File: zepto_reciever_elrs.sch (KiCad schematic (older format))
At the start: 50 parts, among them J1 u.fl, SW1 SW_Push, U1 STM32WLE5JBI6, U2 NCP160, U3 BGS12PL6E6327XTSA1, Y1 32MHz

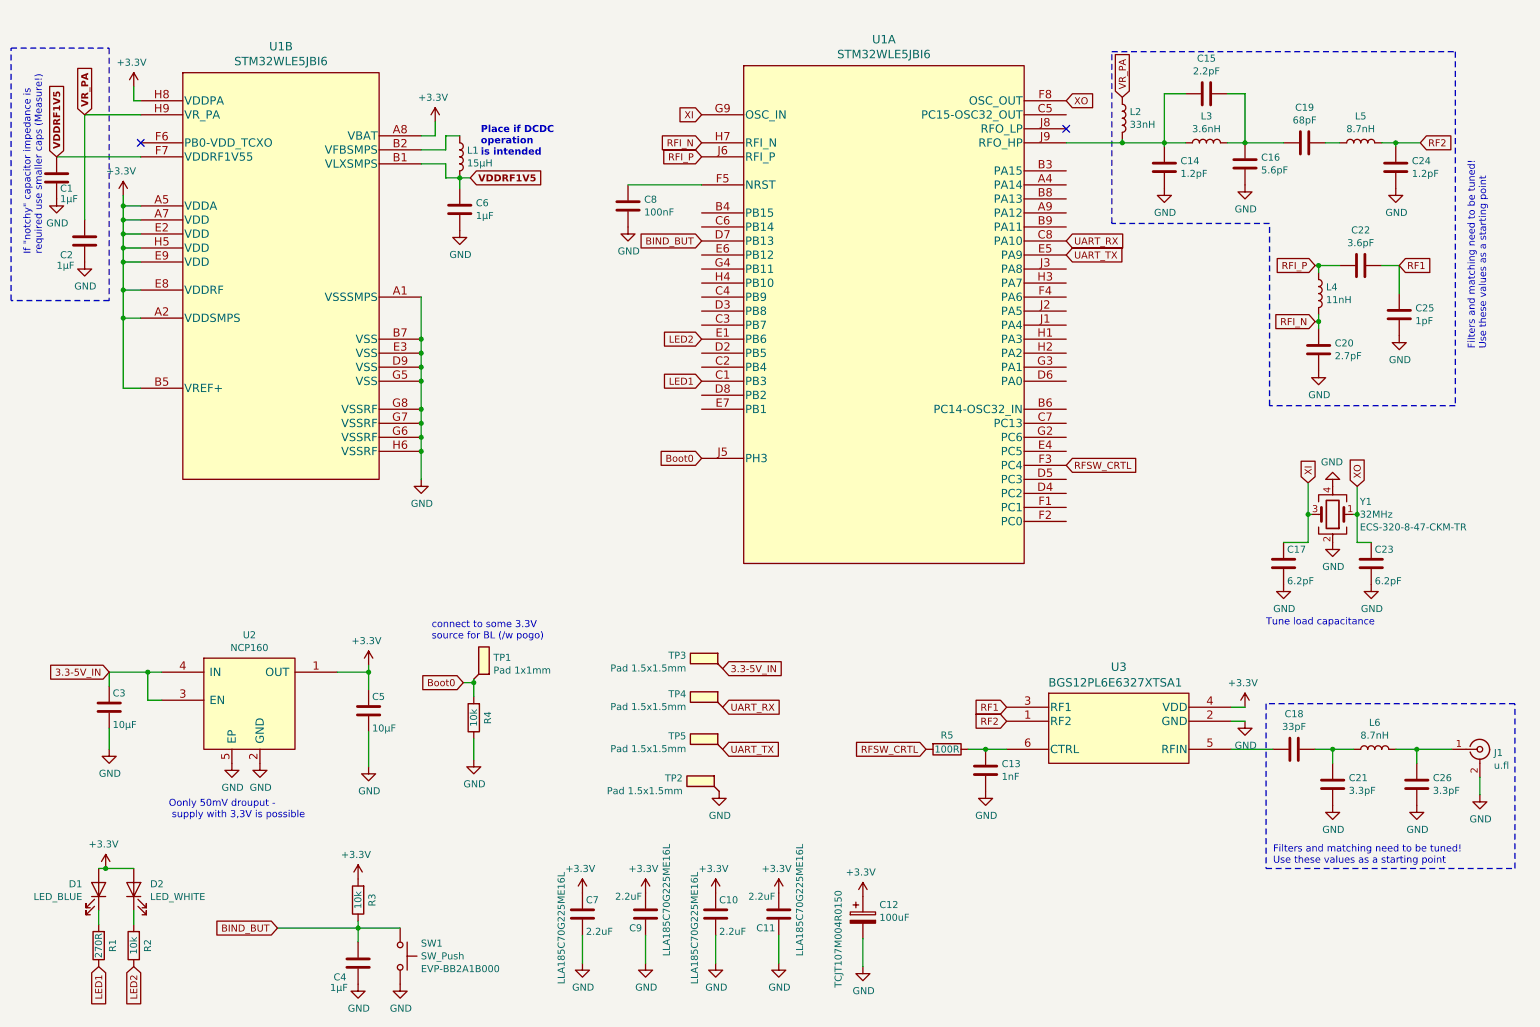
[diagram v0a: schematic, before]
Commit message: Routed half of the Layout, changed a few pins
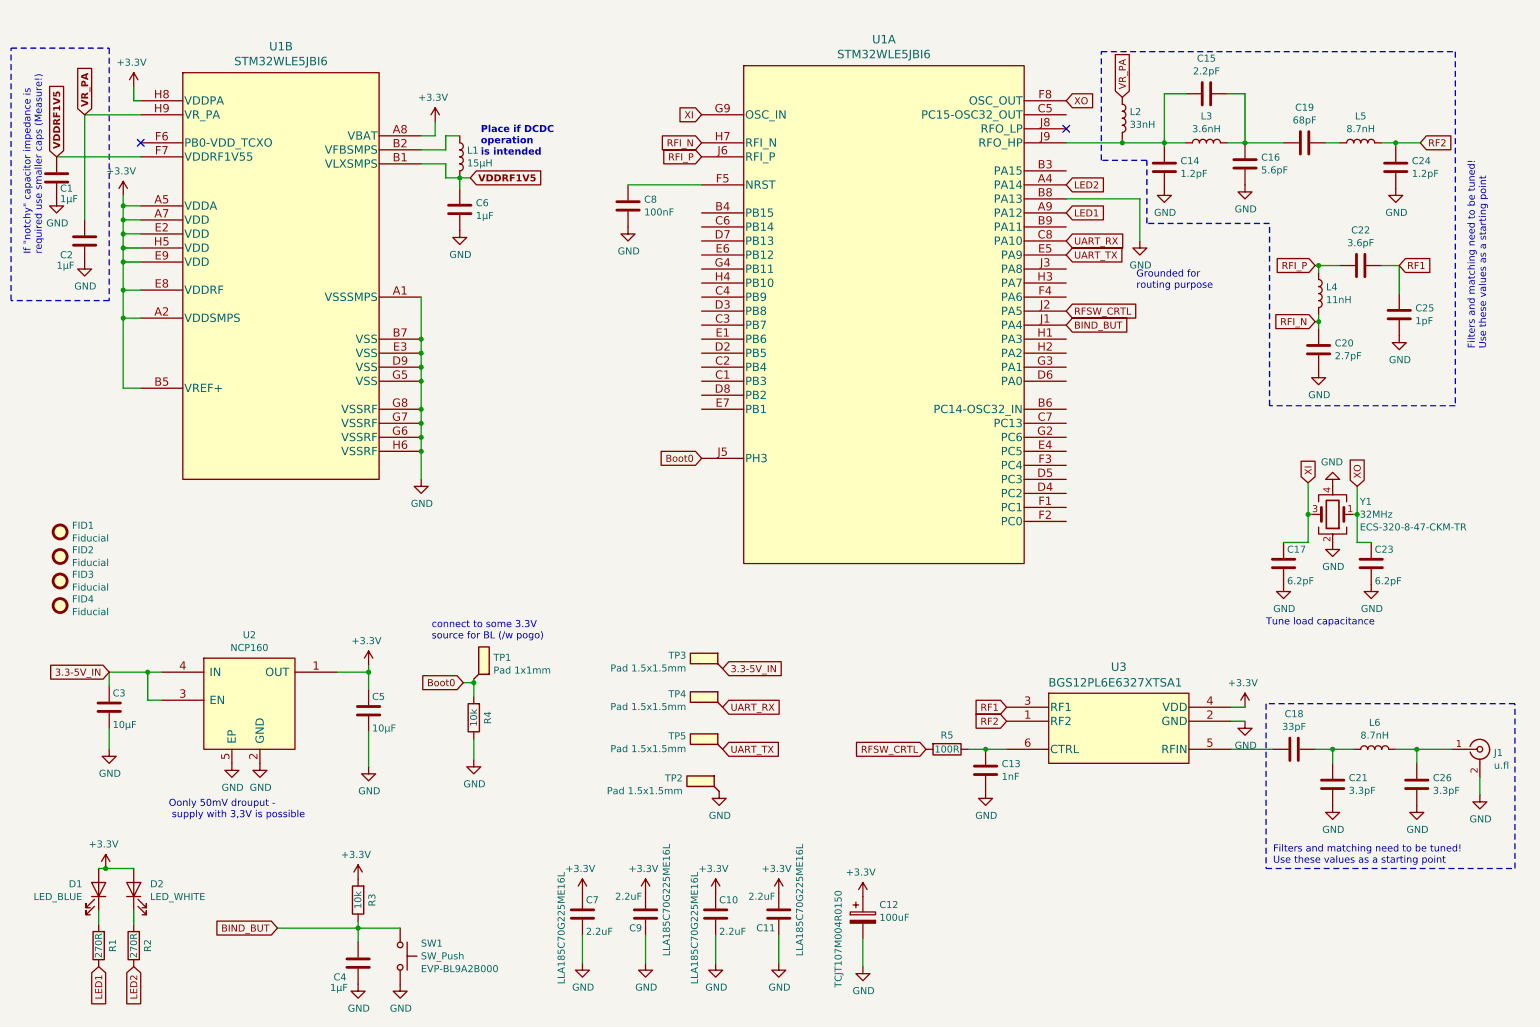
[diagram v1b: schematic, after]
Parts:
- added FID1, FID2, FID3, FID4: Fiducial, Fiducial:Fiducial_0.5mm_Dia_1mm_Outer, symbol Mechanical:Fiducial
- D1: footprint LED_SMD:LED_0201_0603Metric -> LED_SMD:LED_0402_1005Metric; BomCos@10k 0,057 -> 0,059; Type SML-LX0201USBC-TR -> VLMB1500-GS08
- D2: footprint LED_SMD:LED_0201_0603Metric -> LED_SMD:LED_0402_1005Metric; BomCos@10k 0,062 -> 0,053; Type SML-LX0201NWD-TR -> LW QH8G-Q2OO-3K5L-1
- L1: footprint Inductor_SMD:L_0805_2012Metric -> Inductor_SMD:L_0603_1608Metric_Pad1.05x0.95mm_HandSolder; BomCos@10k 0,032 -> 0,103; Type MLZ2012N150LT000 -> BRL1608T150M
- R1: Type RC0201FR-0710KL -> RC0201FR-07270RL
- R2: value 10k -> 270R; Type RC0201FR-0710KL -> RC0201FR-07270RL
- SW1: footprint ftprnts:SW_EVP-BB2A9B000 -> ftprnts:EVPBL9A2B000; Type EVP-BB2A1B000 -> EVP-BL9A2B000
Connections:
- net BIND_BUT: now also U1.J1 (PA4); no longer U1.D7 (PB13)
- net GND: now also U1.B8 (PA13)
- net LED1: now also U1.A9 (PA12); no longer U1.C1 (PB3)
- net LED2: now also U1.A4 (PA14); no longer U1.E1 (PB6)
- net RFSW_CRTL: now also U1.J2 (PA5); no longer U1.F3 (PC4)
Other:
- note added: "Grounded for \nrouting purpose"
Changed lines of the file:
@@
 EESchema Schematic File Version 4
+LIBS:zepto_reciever_elrs-cache
 EELAYER 30 0
 EELAYER END
@@
 Wire Wire Line
 	1150 6525 1350 6525
-Text GLabel 5400 3050 0    50   Input ~ 0
+Text GLabel 8000 1850 2    50   Input ~ 0
 LED1
-Text GLabel 5400 2750 0    50   Input ~ 0
+Text GLabel 8000 1650 2    50   Input ~ 0
 LED2
 $Comp
@@
 Text GLabel 7000 5675 0    50   Input ~ 0
 RFSW_CRTL
-Text GLabel 8000 3650 2    50   Input ~ 0
+Text GLabel 8000 2550 2    50   Input ~ 0
 RFSW_CRTL
 Text Notes 11000 2825 1    50   ~ 0
@@
 Wire Notes Line
 	9450 3225 9450 1925
-Wire Notes Line
-	9450 1925 8325 1925
-Wire Notes Line
-	8325 1925 8325 700
-Wire Notes Line
-	8325 700  10775 700
 Wire Wire Line
 	2950 6900 2950 6950
@@
 	1    0    0    -1
 $EndComp
-Text GLabel 5400 2050 0    50   Input ~ 0
+Text GLabel 8000 2650 2    50   Input ~ 0
 BIND_BUT
 $Comp
@@
 F 3 "~" H 1100 7075 50  0001 C CNN
 F 4 "0,003" H 1100 7075 50  0001 C CNN "BomCos@10k"
-F 5 "RC0201FR-0710KL " H 1100 7075 50  0001 C CNN "Type"
+F 5 "RC0201FR-07270RL" H 1100 7075 50  0001 C CNN "Type"
 	1    1100 7075
 	-1   0    0    1
@@
 F 0 "D2" V 1389 6558 50  0000 R CNN
 F 1 "LED_WHITE" V 1298 6558 50  0000 R CNN
-F 2 "LED_SMD:LED_0201_0603Metric" H 1350 6675 50  0001 C CNN
+F 2 "LED_SMD:LED_0402_1005Metric" H 1350 6675 50  0001 C CNN
 F 3 "~" H 1350 6675 50  0001 C CNN
-F 4 "0,062" H 1350 6675 50  0001 C CNN "BomCos@10k"
-F 5 "SML-LX0201NWD-TR" H 1350 6675 50  0001 C CNN "Type"
+F 4 "0,053" H 1350 6675 50  0001 C CNN "BomCos@10k"
+F 5 "LW QH8G-Q2OO-3K5L-1 " H 1350 6675 50  0001 C CNN "Type"
 	1    1350 6675
 	0    -1   -1   0
@@
 F 0 "SW1" V 3159 7298 50  0000 L CNN
 F 1 "SW_Push" V 3250 7298 50  0000 L CNN
-F 2 "ftprnts:SW_EVP-BB2A9B000" H 3250 7350 50  0001 C CNN
+F 2 "ftprnts:EVPBL9A2B000" H 3250 7350 50  0001 C CNN
 F 3 "~" H 3250 7350 50  0001 C CNN
-F 4 "EVP-BB2A1B000" V 3341 7298 50  0000 L CNN "Type"
+F 4 "EVP-BL9A2B000 " V 3341 7298 50  0000 L CNN "Type"
 	1    3250 7150
 	0    1    1    0
@@
 F 0 "L1" H 3727 1496 50  0000 L CNN
 F 1 "15µH" H 3727 1405 50  0000 L CNN
-F 2 "Inductor_SMD:L_0805_2012Metric" H 3675 1450 50  0001 C CNN
+F 2 "Inductor_SMD:L_0603_1608Metric_Pad1.05x0.95mm_HandSolder" H 3675 1450 50  0001 C CNN
 F 3 "~" H 3675 1450 50  0001 C CNN
-F 4 "MLZ2012N150LT000" H 3675 1450 50  0001 C CNN "Type"
-F 5 "0,032" H 3675 1450 50  0001 C CNN "BomCos@10k"
+F 4 "BRL1608T150M" H 3675 1450 50  0001 C CNN "Type"
+F 5 "0,103" H 3675 1450 50  0001 C CNN "BomCos@10k"
 	1    3675 1450
 	1    0    0    -1
@@
 F 0 "D1" V 1139 6558 50  0000 R CNN
 F 1 "LED_BLUE" V 1048 6558 50  0000 R CNN
-F 2 "LED_SMD:LED_0201_0603Metric" H 1100 6675 50  0001 C CNN
+F 2 "LED_SMD:LED_0402_1005Metric" H 1100 6675 50  0001 C CNN
 F 3 "~" H 1100 6675 50  0001 C CNN
-F 4 "0,057" H 1100 6675 50  0001 C CNN "BomCos@10k"
-F 5 "SML-LX0201USBC-TR" H 1100 6675 50  0001 C CNN "Type"
+F 4 "0,059" H 1100 6675 50  0001 C CNN "BomCos@10k"
+F 5 "VLMB1500-GS08" H 1100 6675 50  0001 C CNN "Type"
 	1    1100 6675
 	0    1    -1   0
@@
 P 1350 7075
 F 0 "R2" V 1250 7075 50  0000 C CNN
-F 1 "10k" V 1350 7075 50  0000 C CNN
+F 1 "270R" V 1350 7075 50  0000 C CNN
 F 2 "Resistor_SMD:R_0201_0603Metric" V 1280 7075 50  0001 C CNN
 F 3 "~" H 1350 7075 50  0001 C CNN
 F 4 "0,003" H 1350 7075 50  0001 C CNN "BomCos@10k"
-F 5 "RC0201FR-0710KL " H 1350 7075 50  0001 C CNN "Type"
+F 5 "RC0201FR-07270RL" H 1350 7075 50  0001 C CNN "Type"
 	1    1350 7075
 	-1   0    0    1
 $EndComp
+$Comp
+L Mechanical:Fiducial FID1
+U 1 1 6049244C
+P 825 4125
+F 0 "FID1" H 910 4171 50  0000 L CNN
+F 1 "Fiducial" H 910 4080 50  0000 L CNN
+F 2 "Fiducial:Fiducial_0.5mm_Dia_1mm_Outer" H 825 4125 50  0001 C CNN
+F 3 "~" H 825 4125 50  0001 C CNN
+	1    825  4125
+	1    0    0    -1
+$EndComp
+$Comp
+L Mechanical:Fiducial FID2
+U 1 1 60493583
+P 825 4300
+F 0 "FID2" H 910 4346 50  0000 L CNN
+F 1 "Fiducial" H 910 4255 50  0000 L CNN
+F 2 "Fiducial:Fiducial_0.5mm_Dia_1mm_Outer" H 825 4300 50  0001 C CNN
+F 3 "~" H 825 4300 50  0001 C CNN
+	1    825  4300
+	1    0    0    -1
+$EndComp
+$Comp
+L Mechanical:Fiducial FID3
+U 1 1 60493677
+P 825 4475
+F 0 "FID3" H 910 4521 50  0000 L CNN
+F 1 "Fiducial" H 910 4430 50  0000 L CNN
+F 2 "Fiducial:Fiducial_0.5mm_Dia_1mm_Outer" H 825 4475 50  0001 C CNN
+F 3 "~" H 825 4475 50  0001 C CNN
+	1    825  4475
+	1    0    0    -1
+$EndComp
+$Comp
+L Mechanical:Fiducial FID4
+U 1 1 6049379B
+P 825 4650
+F 0 "FID4" H 910 4696 50  0000 L CNN
+F 1 "Fiducial" H 910 4605 50  0000 L CNN
+F 2 "Fiducial:Fiducial_0.5mm_Dia_1mm_Outer" H 825 4650 50  0001 C CNN
+F 3 "~" H 825 4650 50  0001 C CNN
+	1    825  4650
+	1    0    0    -1
+$EndComp
+$Comp
+L power:GND #PWR0101
+U 1 1 6051D24B
+P 8525 2050
+F 0 "#PWR0101" H 8525 1800 50  0001 C CNN
+F 1 "GND" H 8530 1877 50  0000 C CNN
+F 2 "" H 8525 2050 50  0001 C CNN
+F 3 "" H 8525 2050 50  0001 C CNN
+	1    8525 2050
+	1    0    0    -1
+$EndComp
+Wire Wire Line
+	8000 1750 8525 1750
+Wire Wire Line
+	8525 1750 8525 2050
+Text Notes 8500 2400 0    50   ~ 0
+Grounded for \nrouting purpose
+Wire Notes Line
+	9450 1925 8575 1925
+Wire Notes Line
+	8575 1925 8575 1475
+Wire Notes Line
+	8575 1475 8250 1475
+Wire Notes Line
+	8250 1475 8250 700
+Wire Notes Line
+	8250 700  10775 700
 $EndSCHEMATC
